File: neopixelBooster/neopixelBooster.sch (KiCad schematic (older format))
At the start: 24 parts, among them J1 +12, J2 +12, J3 GND, J4 GND, J5 ESP_INPUT, P1 NeopixelStripPads, P2 NeopixelStripPads, U1 SY8105

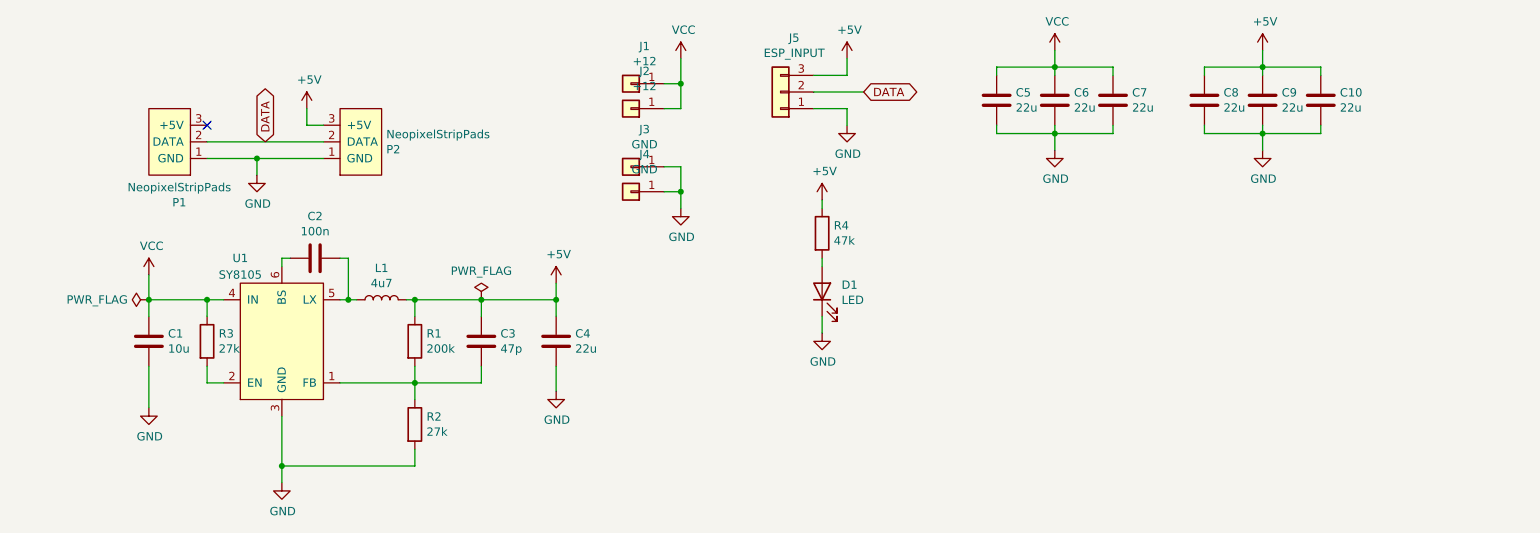
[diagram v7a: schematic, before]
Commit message: Fixed polygon priority, add voltage of capacitors to schematic
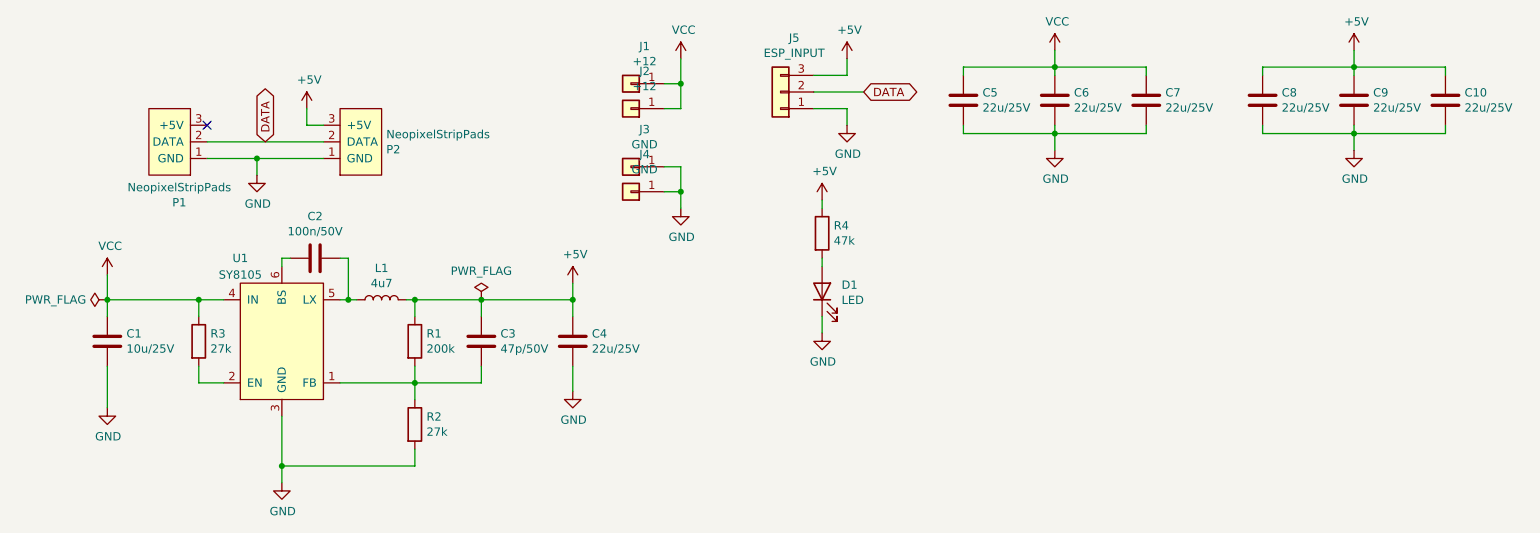
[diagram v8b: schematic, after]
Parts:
- C1: value 10u -> 10u/25V
- C10, C4, C5, C6, C7, C8, C9: value 22u -> 22u/25V
- C2: value 100n -> 100n/50V
- C3: value 47p -> 47p/50V
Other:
- moved on the sheet: C1, C10, C4, C5, C7, C8, C9, R3
